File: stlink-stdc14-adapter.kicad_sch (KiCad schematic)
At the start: 7 parts, among them J1 Conn_ST_STDC14, J2 Conn_ARM_JTAG_SWD_20, J3 Conn_01x04

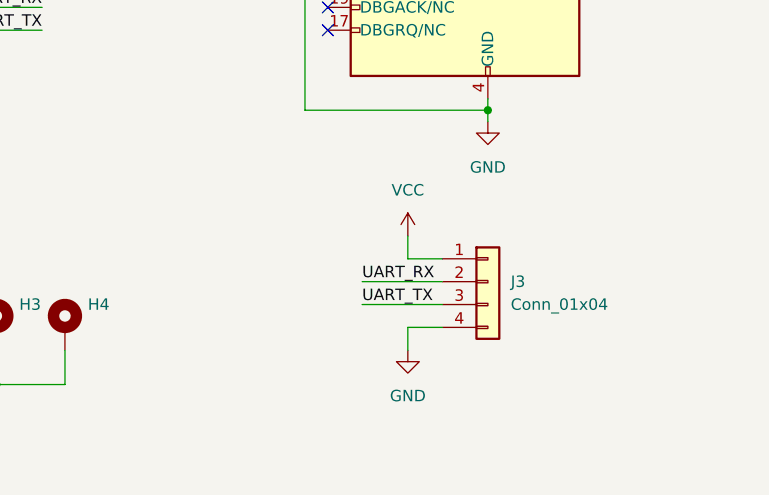
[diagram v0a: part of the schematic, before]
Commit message: swap RX and TX on the UART header
Yep, I was wrong on the 50/50 guess, as is tradition.
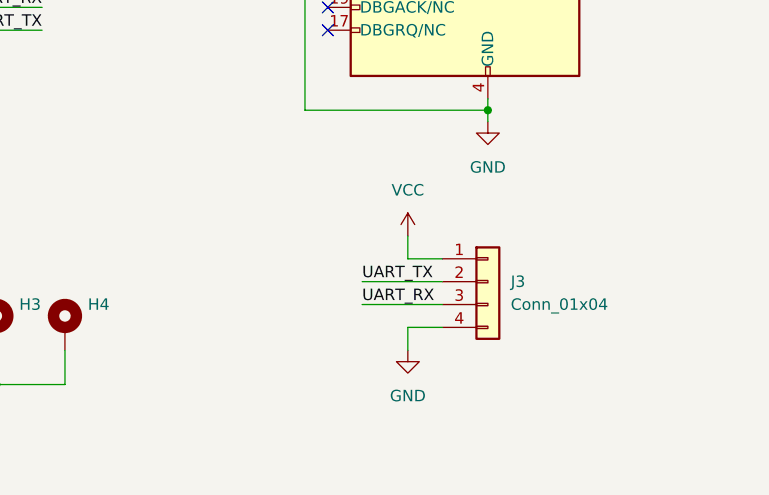
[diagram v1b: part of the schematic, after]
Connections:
- net UART_RX: now also J3.3 (Pin_3); no longer J3.2 (Pin_2)
- net UART_TX: now also J3.2 (Pin_2); no longer J3.3 (Pin_3)
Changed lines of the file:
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@@
 		)
 	)
-	(label "UART_RX"
+	(label "UART_TX"
 		(at 114.3 114.3 0)
 		(effects
@@
 		)
 	)
-	(label "UART_TX"
+	(label "UART_RX"
 		(at 114.3 116.84 0)
 		(effects

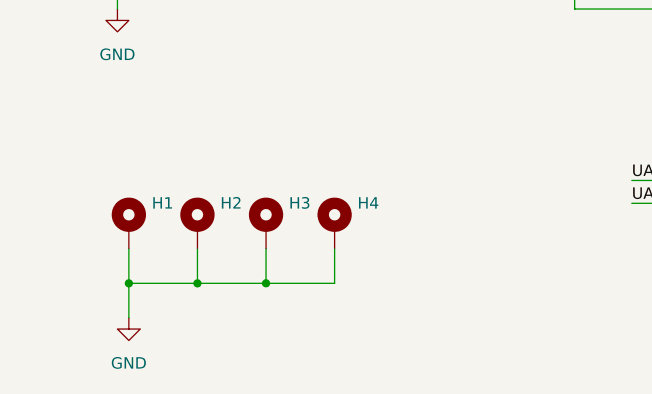
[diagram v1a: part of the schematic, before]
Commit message: kinda redo the whole layout for a smaller board
1.5" x 1" size, no more mounting holes. Smaller = cheaper.
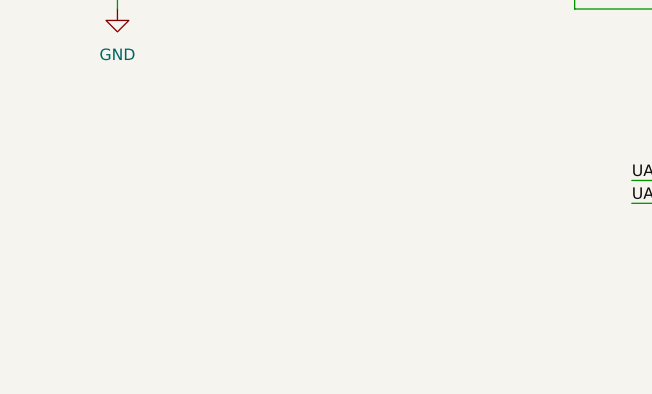
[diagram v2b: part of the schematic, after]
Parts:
- removed H1, H2, H3, H4: MountingHole_Pad, MountingHole:MountingHole_3.2mm_M3_Pad, symbol Mechanical:MountingHole_Pad

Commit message: re-route, add silkscreen and via stitching
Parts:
- J2: footprint Connector_PinSocket_2.54mm:PinSocket_2x10_P2.54mm_Vertical -> Connector_IDC:IDC-Header_2x10_P2.54mm_Vertical
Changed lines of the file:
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@@
 			)
 		)
-		(property "Footprint" "Connector_PinSocket_2.54mm:PinSocket_2x10_P2.54mm_Vertical"
+		(property "Footprint" "Connector_IDC:IDC-Header_2x10_P2.54mm_Vertical"
 			(at 114.3 100.33 0)
 			(hide yes)
